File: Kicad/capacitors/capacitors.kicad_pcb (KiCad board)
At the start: 2 copper layers, 100 x 35 mm, 142 parts, among them K1 Capacitor

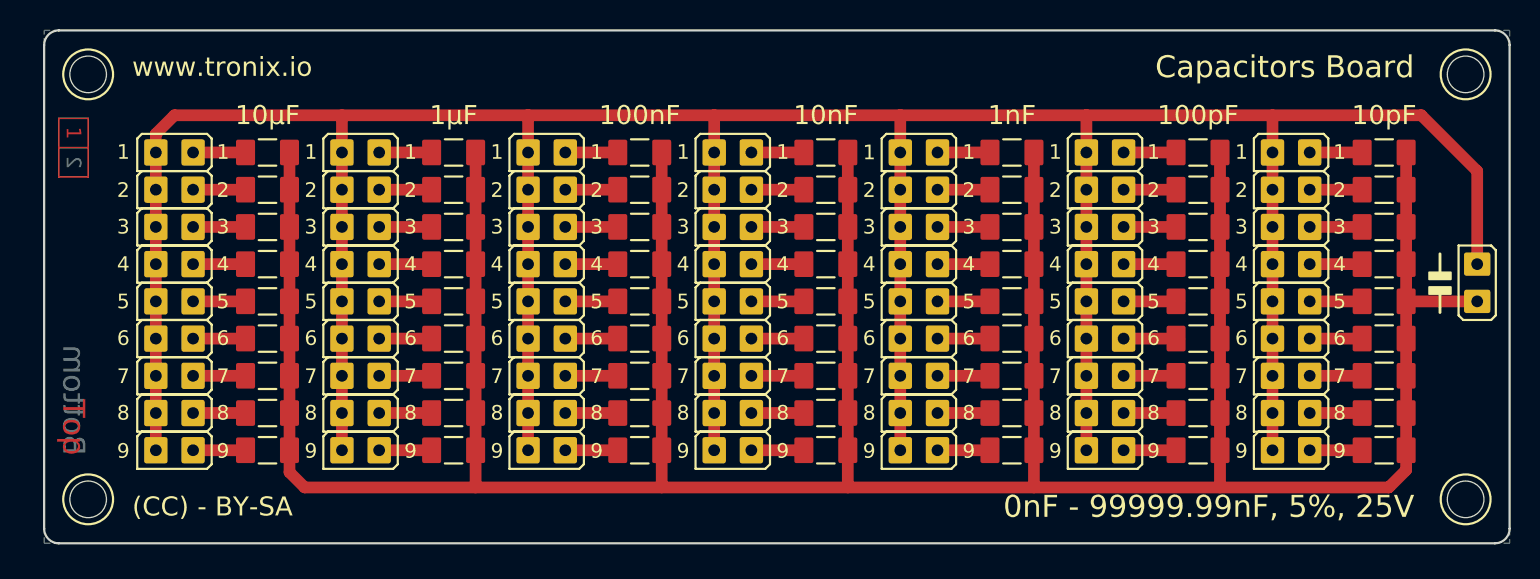
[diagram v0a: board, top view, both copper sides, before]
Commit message: Update capacitors
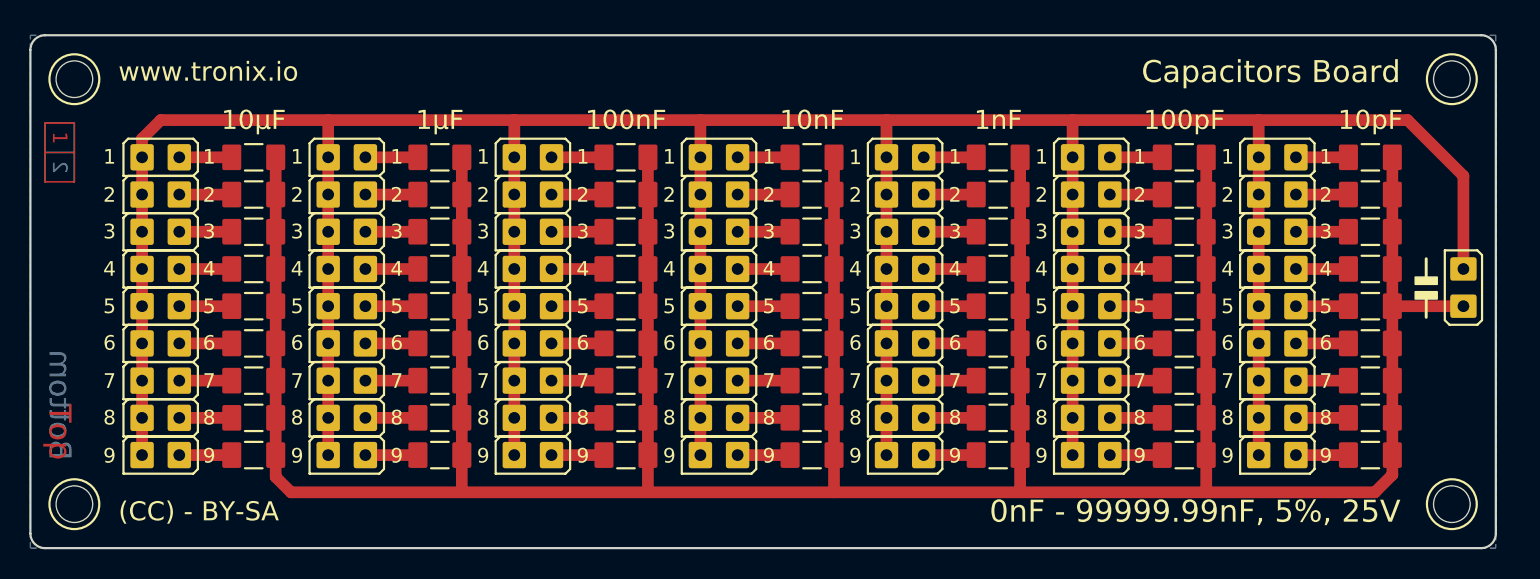
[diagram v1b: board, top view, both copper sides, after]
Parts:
- H1, H2, H3, H4: value KEYSTONE-9056 -> 9056
- JP1, JP10, JP11, JP12, JP13, JP14, JP15, JP16, JP17, JP18, JP19, JP2, JP20, JP21, JP22, JP23, JP24, JP25, JP26, JP27, JP28, JP29, JP3, JP30, JP31, JP32, JP33, JP34, JP35, JP36, JP37, JP38, JP39, JP4, JP40, JP41, JP42, JP43, JP44, JP45, JP46, JP47, JP48, JP49, JP5, JP50, JP51, JP52, JP53, JP54, JP55, JP56, JP57, JP58, JP59, JP6, JP60, JP61, JP62, JP63, JP7, JP8, JP9: value HARWIN-254-M-1X02-JUMPER-VERTICAL -> ~
- moved C16 1.00 mm to (127.0, 88.9)
- moved C25 1.00 mm to (139.7, 88.9)
- moved C34 1.00 mm to (152.4, 88.9)
- moved C43 1.00 mm to (165.1, 88.9)
- moved C52 1.00 mm to (177.8, 88.9)
- moved C61 1.00 mm to (190.5, 88.9)
- moved C7 1.00 mm to (114.3, 88.9)
- moved JP16 1.00 mm to (119.4, 88.9)
- moved JP25 1.00 mm to (132.1, 88.9)
- moved JP34 1.00 mm to (144.8, 88.9)
- moved JP43 1.00 mm to (157.5, 88.9)
- moved JP52 1.00 mm to (170.2, 88.9)
- moved JP61 1.00 mm to (182.9, 88.9)
- moved JP7 1.00 mm to (106.7, 88.9)
- moved C1 1.00 mm to (114.3, 73.7)
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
